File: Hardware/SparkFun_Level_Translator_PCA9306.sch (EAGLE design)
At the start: 18 parts, among them U1 PCA9306

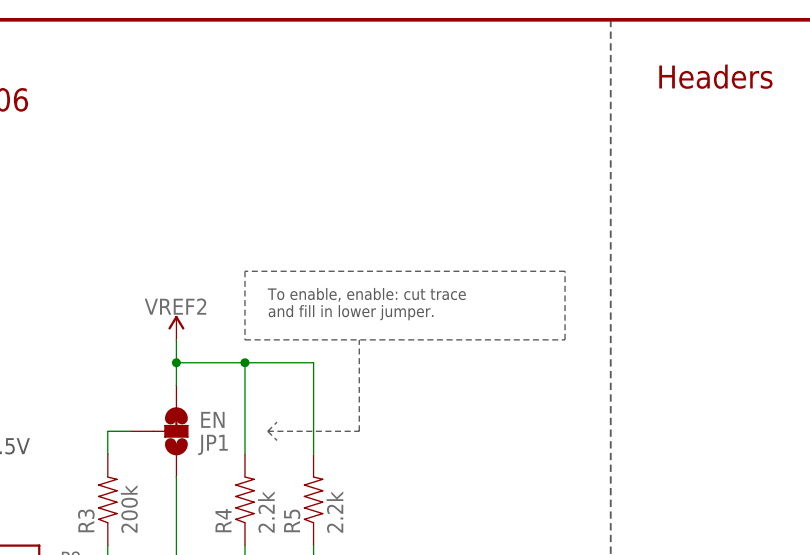
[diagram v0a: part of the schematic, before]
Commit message: Updates enable text in schematic
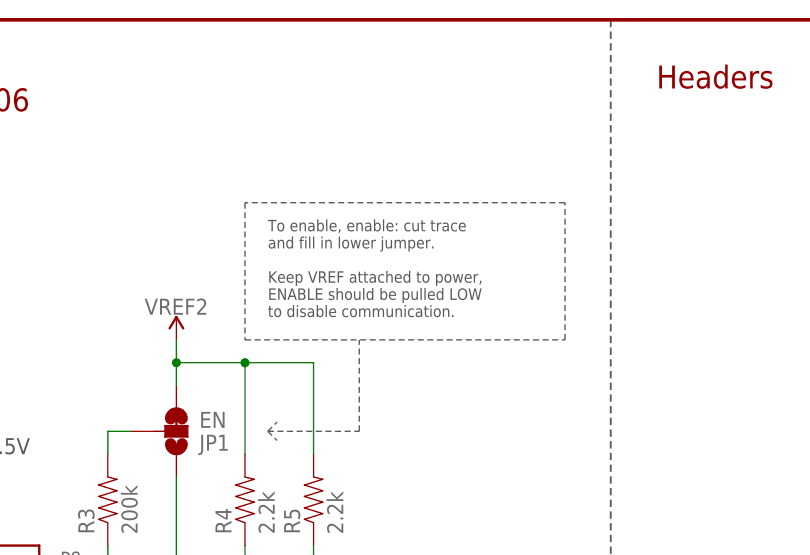
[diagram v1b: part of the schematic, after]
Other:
- note added: "Keep VREF attached to power, ENABLE should be pulled LOW to disable communication."
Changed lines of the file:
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@@
 <text x="68.58" y="38.1" size="2.54" layer="97" font="vector">5V</text>
 <text x="33.02" y="137.16" size="1.778" layer="97" font="vector">VCC Range: 1.2 - 5.5V</text>
-<text x="83.82" y="152.4" size="1.27" layer="97" font="vector">To enable, enable: cut trace
+<text x="83.82" y="160.02" size="1.27" layer="97" font="vector">To enable, enable: cut trace
 and fill in lower jumper.</text>
 <wire x1="83.82" y1="139.7" x2="93.98" y2="139.7" width="0.1524" layer="97" style="dashdot"/>
 <wire x1="93.98" y1="139.7" x2="93.98" y2="149.86" width="0.1524" layer="97" style="dashdot"/>
-<wire x1="81.28" y1="157.48" x2="81.28" y2="149.86" width="0.1524" layer="97" style="dashdot"/>
+<wire x1="81.28" y1="165.1" x2="81.28" y2="149.86" width="0.1524" layer="97" style="dashdot"/>
 <wire x1="81.28" y1="149.86" x2="116.84" y2="149.86" width="0.1524" layer="97" style="dashdot"/>
-<wire x1="116.84" y1="149.86" x2="116.84" y2="157.48" width="0.1524" layer="97" style="dashdot"/>
-<wire x1="116.84" y1="157.48" x2="81.28" y2="157.48" width="0.1524" layer="97" style="dashdot"/>
+<wire x1="116.84" y1="149.86" x2="116.84" y2="165.1" width="0.1524" layer="97" style="dashdot"/>
+<wire x1="116.84" y1="165.1" x2="81.28" y2="165.1" width="0.1524" layer="97" style="dashdot"/>
 <wire x1="83.82" y1="139.7" x2="84.836" y2="140.716" width="0.1524" layer="97" style="dashdot"/>
 <wire x1="83.82" y1="139.7" x2="84.836" y2="138.684" width="0.1524" layer="97" style="dashdot"/>
+<text x="83.82" y="152.4" size="1.27" layer="97" font="vector">Keep VREF attached to power,
+ENABLE should be pulled LOW
+to disable communication.</text>
 </plain>
 <instances>
